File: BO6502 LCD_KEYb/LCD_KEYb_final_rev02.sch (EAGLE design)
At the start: 20 parts, among them IC1 74HCT14N, IC2 74HCT595N, IC3 74HCT595N, IC4 74AC138N, U1 65C22, X1 DIN 5 pin

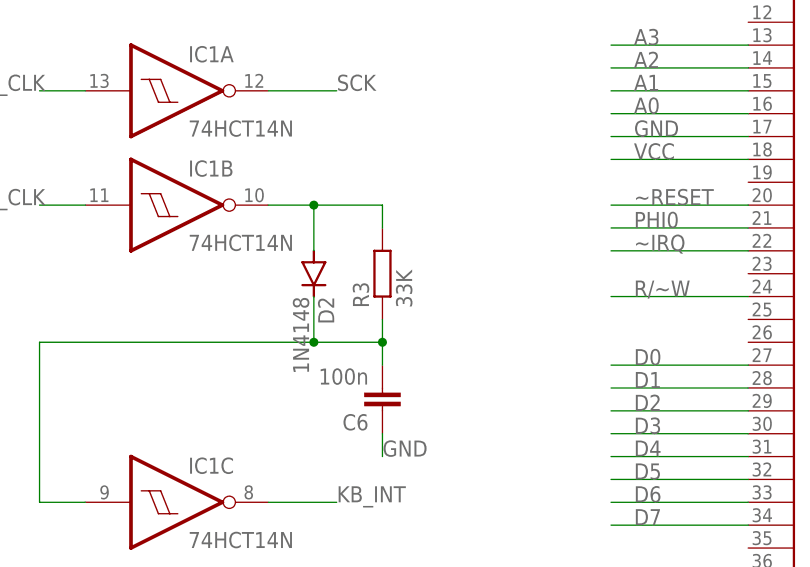
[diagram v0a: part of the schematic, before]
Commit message: R3 wrong value
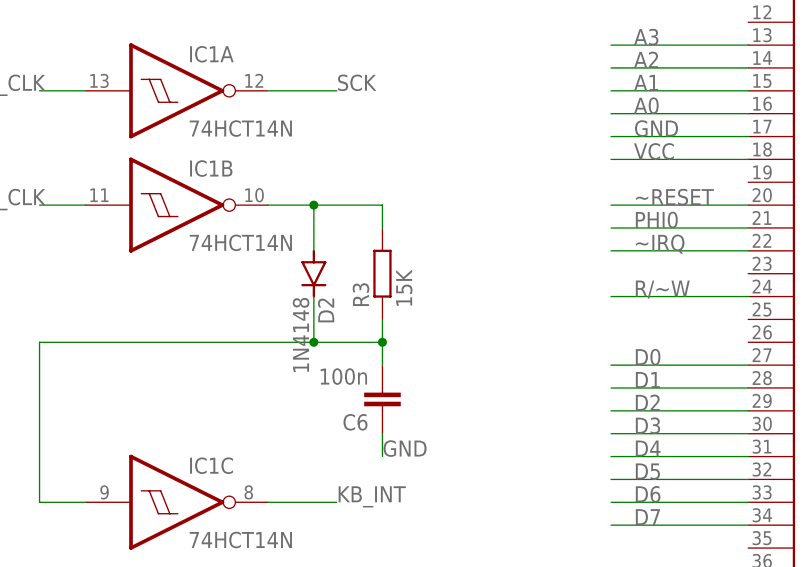
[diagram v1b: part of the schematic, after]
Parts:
- R3: value 33K -> 15K
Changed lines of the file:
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@@
 <part name="IC3" library="74xx-eu" library_urn="urn:adsk.eagle:library:85" deviceset="74*595" device="N" package3d_urn="urn:adsk.eagle:package:922/2" technology="HCT"/>
 <part name="X1" library="con-hirschmann_mod" deviceset="MAB5SH" device="" package3d_urn="urn:adsk.eagle:package:7443/1" value="DIN 5 pin"/>
-<part name="R3" library="rcl" library_urn="urn:adsk.eagle:library:334" deviceset="R-EU_" device="0207/10" package3d_urn="urn:adsk.eagle:package:23491/2" value="33K"/>
+<part name="R3" library="rcl" library_urn="urn:adsk.eagle:library:334" deviceset="R-EU_" device="0207/10" package3d_urn="urn:adsk.eagle:package:23491/2" value="15K"/>
 <part name="C6" library="rcl" library_urn="urn:adsk.eagle:library:334" deviceset="C-EU" device="025-025X050" package3d_urn="urn:adsk.eagle:package:23629/2" value="100n"/>
 <part name="D2" library="diode" library_urn="urn:adsk.eagle:library:210" deviceset="1N4148" device="DO35-7" package3d_urn="urn:adsk.eagle:package:43339/2" value="1N4148"/>
